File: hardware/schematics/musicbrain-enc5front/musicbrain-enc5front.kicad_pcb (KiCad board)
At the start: 2 copper layers, 20 x 110 mm, 8 parts, among them J1 SOCKET-BACK, SW1 EC11E, SW2 EC11E, SW3 EC11E, SW4 EC11E, SW5 EC11E, U1 MCP23017-E/ML

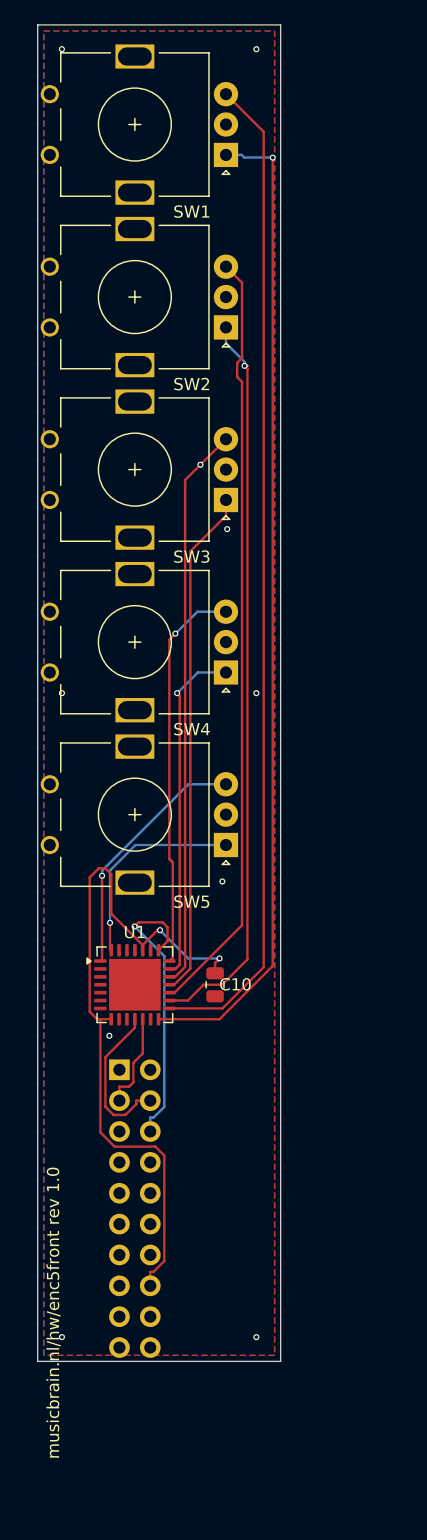
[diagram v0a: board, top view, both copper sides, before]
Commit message: ENC5-FRONT rev 2.0 + i2criser: herontwerp op de front-koppel-standaard
ENC5-FRONT 2.0 (30x110, DRC 0/0 + fab):
- 1x10-socket op de front-koppel-standaard (x=116,5 / pin1 y=143,57) i.p.v.
  de 2x10-riser-socket middenop (paste mechanisch niet - besluit Mark)
- encoders 90 graden gedraaid (socketkolom vrij), steek 17,6, hartlijn 8,0;
  bord 30 mm breed (front zit uiterst links/rechts in het paneel)
- 2x MCP23017 (0x20/0x21) = 32 bits: drukassen bedraad, 2 knopjes terug,
  2x8-expansieheader voor display-deel (2 encoders + 4 knoppen + 2 spares)
- routing: freerouting-pijplijn (beste-van-N-lus), clearance 0,15-netclass,
  X_E7S handroute; netcheck + DRC 0/0

Nieuw bord musicbrain-i2criser rev 1.0 (DRC 0/0 + fab): domme I2C-doorlus
slot -> 1x10-front (potriser-mechanica, geen componenten).

Toolkit: cardlib paper-instelling + PNET-registratie + snap_stubs();
seslib apply_ses(only=/skip=); make_fab bordenlijst + i2criser.
README's: enc5front herschreven, i2criser nieuw, jack8/jack4/pot8front/
riser bijgewerkt (versies + standaard + riser-familie).

Co-Authored-By: Claude Fable 5 <noreply@anthropic.com>
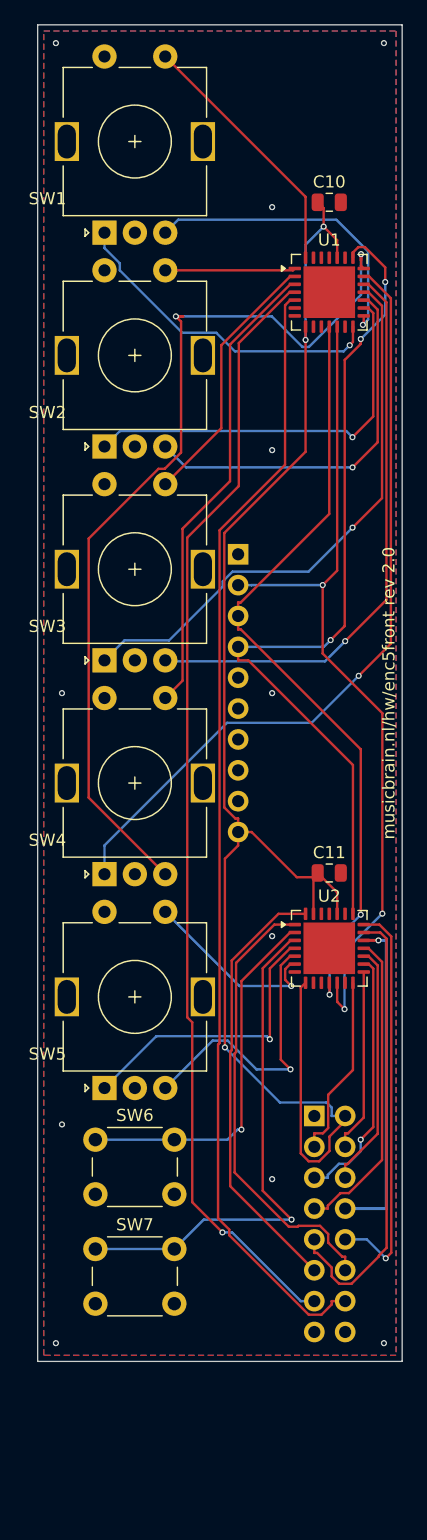
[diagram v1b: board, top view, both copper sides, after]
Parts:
- added C10: 100n, Capacitor_SMD:C_0805_2012Metric, F.Cu at (124.0, 114.6)
- added C11: 100n, Capacitor_SMD:C_0805_2012Metric, F.Cu at (124.0, 169.8)
- added J1: Socket_1x10_backside, MusicBrain:Socket_1x10_backside, B.Cu at (116.5, 143.6)
- added J2: Header_2x08_backside, MusicBrain:Header_2x08_backside, B.Cu at (122.8, 189.8)
- added U2: MCP23017-E/ML, Package_DFN_QFN:QFN-28-1EP_6x6mm_P0.65mm_EP4.25x4.25mm, F.Cu at (124.0, 176.0)
- SW6: renamed from U1; value MCP23017-E/ML -> 6mm tact; footprint Package_DFN_QFN:QFN-28-1EP_6x6mm_P0.65mm_EP4.25x4.25mm -> Button_Switch_THT:SW_PUSH_6mm
- SW7: renamed from C10; value 100n -> 6mm tact; footprint Capacitor_SMD:C_0805_2012Metric -> Button_Switch_THT:SW_PUSH_6mm
- U1: renamed from J1; value SOCKET-BACK -> MCP23017-E/ML; footprint MusicBrain:Socket_2x10_backside -> Package_DFN_QFN:QFN-28-1EP_6x6mm_P0.65mm_EP4.25x4.25mm; moved to F.Cu
- moved U1 66.0 mm to (124.0, 122.0)
- moved SW7 23.9 mm to (104.8, 200.8), turned to 0 degrees
- moved SW5 22.4 mm to (105.5, 187.5), turned to 90 degrees
- moved SW4 19.4 mm to (105.5, 169.9), turned to 90 degrees
- moved SW3 16.6 mm to (105.5, 152.3), turned to 90 degrees
- moved SW2 14.0 mm to (105.5, 134.7), turned to 90 degrees
- moved SW6 13.2 mm to (104.8, 191.8)
- moved SW1 11.9 mm to (105.5, 117.1), turned to 90 degrees
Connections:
- SW1 pad S1: (no net) -> /E1S
- SW1 pad S2: (no net) -> GND
- SW2 pad S1: (no net) -> /E2S
- SW2 pad S2: (no net) -> GND
- SW3 pad S1: (no net) -> /E3S
- SW3 pad S2: (no net) -> GND
- SW4 pad S1: (no net) -> /E4S
- SW4 pad S2: (no net) -> GND
- SW5 pad S1: (no net) -> /E5S
- SW5 pad S2: (no net) -> GND
- SW6 pad 1: /E5B -> /K1
- SW6 pad 2: (no net) -> GND
- SW7 pad 1: +3V3 -> /K2
- U1 pad 1: (no net) -> /E2S
- U1 pad 10: GND -> (no net)
- U1 pad 11: (no net) -> /SCL
- U1 pad 12: GND -> /SDA
- U1 pad 14: GND -> /E1A
- U1 pad 15: GND -> /E1B
- U1 pad 16: +3V3 -> /E2A
- U1 pad 17: GND -> /E2B
- U1 pad 18: (no net) -> /E3A
- U1 pad 19: GND -> /E3B
- U1 pad 2: (no net) -> /E3S
- U1 pad 20: (no net) -> /E4A
- U1 pad 3: /SDA -> /E4S
- U1 pad 4: /SCL -> /X_SP1
- U1 pad 5: (no net) -> /X_SP2
- U1 pad 6: /IRQ -> (no net)
- U1 pad 8: GND -> +3V3
- U1 pad 9: (no net) -> GND
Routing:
- net /X_SP2: track 0.00 -> 93.1 mm
- net /X_SP1: track 0.00 -> 92.4 mm, vias 0 -> 1
- net +3V3: track 60.8 -> 126.8 mm, vias 2 -> 3
- net /SDA: track 7.96 -> 69.4 mm, vias 0 -> 3
- net /E1B: track 82.3 -> 25.2 mm, vias 0 -> 1
- net /E1A: track 81.7 -> 27.2 mm
- net /SCL: track 12.8 -> 64.6 mm, vias 0 -> 2
- net /E4B: track 32.5 -> 78.3 mm, vias 1 -> 2
- net /IRQ: track 25.1 -> 70.7 mm, vias 1 -> 3
- net /K2: track 0.00 -> 42.4 mm, vias 0 -> 1
- net /E4S: track 0.00 -> 38.7 mm
- net /X_K1: track 0.00 -> 37.3 mm
- net /X_K4: track 0.00 -> 37.0 mm
- net /X_K3: track 0.00 -> 36.1 mm
- net /E4A: track 28.2 -> 64.2 mm
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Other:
- board size 20 x 110 mm -> 30 x 110 mm
- board text added: "musicbrain.nl/hw/enc5front rev 2.0"
- board text removed: "musicbrain.nl/hw/enc5front rev 1.0"
